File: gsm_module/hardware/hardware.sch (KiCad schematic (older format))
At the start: 33 parts, among them J1 Screw_Terminal_01x04, J2 Programming interface, J3 SWD Debugging Interface, U1 XL1509-5.0, U2 STM32F030F4Px, U3 SIM800C, U4 AMS1117-3.3

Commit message: all but the CANSTACK
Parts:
- removed C10: 100nF, symbol Device:C
- removed C11: 10pF, symbol Device:C
- removed C12: 33pF, symbol Device:C
- removed C9: 330uF, symbol Device:C
- removed R11: 82k, symbol Device:R
- removed U3: SIM800C, RF_GSM:SIMCom_SIM800C, symbol RF_GSM:SIM800C
- added C1, C2: 3.3n, symbol Device:C
- added C4: 100uF, symbol pspice:CAP
- added D2: 1N5820, Diode_THT:D_DO-201AD_P15.24mm_Horizontal, symbol Diode:1N5820
- added D3, D4, D5: LED, symbol Device:LED
- added J2, J3: Conn_01x06_Female, symbol Connector:Conn_01x06_Female
- added JP1, JP2: Jumper, symbol Device:Jumper
- added L2: 68uH, symbol pspice:INDUCTOR
- added R1, R2: 1k, symbol Device:R
- added R13: 100k, symbol Device:R
- added R14: 22k, symbol Device:R
- added R3: 320, symbol Device:R
- added R4: 2.3k, symbol Device:R
- added R5: 330, symbol Device:R
- added U2: XL1509-ADJ, symbol xl1509:XL1509
- added polcap3: 470uF, symbol Device:CP1_Small
- added polcap4: 390uF/6.3v, symbol Device:CP1_Small
- R10: value 100k -> 270k
- R6, R7: value 1k -> 330
- R9: value 330k -> 1k
- U1: value XL1509-5.0 -> XL1509-ADJ
- gave numbers to parts that had none: 2
- renumbered C1 to C3, C4 to C5, C5 to C6, C6 to C7, C7 to C8, C8 to C9, J2 to J4, J3 to J5, JP1 to JP3, JP2 to JP4, R4 to R11, R5 to R12, U4 to U2, U2 to U3
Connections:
- net labels added: 200OK, 4v, NETWORK_ERROR, RESET_PIN, SIM_CARD_ERROR
- wire segments 86 -> 119
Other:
- note removed: "5v to 4V voltage dvider use E12."
- note removed: "ESR=0.7ohm\nsee Hw design p.17 fig.8"
- moved on the sheet: C3, C5, C6, C7, C8, C9, D1, J4, J5, L1, R11, R12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

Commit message: SIM800 Breakout+CANSTACK Rev1 schematic
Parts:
- added C? (x2): 27pF, symbol Device:C
- added JP? (x3): Jumper, symbol Device:Jumper
- added JP?: SPI Jumpers, symbol Device:Jumper
- added R? (x2): 10k, symbol Device:R
- added Y?: 8mhz, symbol Device:Crystal_Small
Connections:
- net labels added: SPI_CSK, SPI_MISO, SPI_MOSI, SPI_NSS
- wire segments 119 -> 136
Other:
- moved on the sheet: C5, C6, C7, C8, C9, J2, J3, J4, J5, R10, R11, R12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

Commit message: Rev 1 schematic all footprints done
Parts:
- removed JP1, JP2, JP? (x3): Jumper, symbol Device:Jumper
- removed JP3, JP4: Programming Jumpers, symbol Device:Jumper
- removed JP?: SPI Jumpers, symbol Device:Jumper
- removed U2: XL1509-ADJ, symbol xl1509:XL1509
- added C11, C5: 5nF, Capacitor_THT:C_Disc_D4.3mm_W1.9mm_P5.00mm, symbol Device:C
- added J10, J11, J12, J13, J6, J7, J8, J9: Conn_01x02_Male, Connector_PinHeader_1.00mm:PinHeader_1x02_P1.00mm_Vertical, symbol Connector:Conn_01x02_Male
- added U10: XL1509-ADJ, Package_SO:SOIC-8-1EP_3.9x4.9mm_P1.27mm_EP2.29x3mm, symbol xl1509:XL1509
- C1, C2: footprint (none) -> Capacitor_THT:C_Disc_D4.3mm_W1.9mm_P5.00mm
- C10: renamed from C9; footprint (none) -> Capacitor_THT:C_Disc_D4.3mm_W1.9mm_P5.00mm
- C12, C13: renamed from C?; footprint (none) -> Capacitor_THT:C_Disc_D4.3mm_W1.9mm_P5.00mm
- C3, C4, polcap1, polcap3, polcap4: footprint (none) -> Capacitor_THT:CP_Radial_D8.0mm_P3.50mm
- C6: renamed from C5; footprint (none) -> Capacitor_THT:C_Disc_D4.3mm_W1.9mm_P5.00mm
- C7: renamed from C6; footprint (none) -> Capacitor_THT:C_Disc_D4.3mm_W1.9mm_P5.00mm
- C8: renamed from C7; footprint (none) -> Capacitor_THT:C_Disc_D4.3mm_W1.9mm_P5.00mm
- C9: renamed from C8; footprint (none) -> Capacitor_THT:C_Disc_D4.3mm_W1.9mm_P5.00mm
- D1, D2: value 1N5820 -> MBR360
- D3, D4, D5: footprint (none) -> LED_THT:LED_D5.0mm
- J1: footprint (none) -> Connector_PinHeader_1.27mm:PinHeader_1x04_P1.27mm_Vertical
- J2: value Conn_01x06_Female -> SIM800C Module; footprint (none) -> Connector_PinHeader_1.27mm:PinHeader_1x06_P1.27mm_Vertical
- J3: value Conn_01x06_Female -> SIM800C Module Side A; footprint (none) -> Connector_PinHeader_1.27mm:PinHeader_1x06_P1.27mm_Vertical
- J4: footprint (none) -> Connector_PinHeader_1.00mm:PinHeader_1x05_P1.00mm_Vertical
- J5: footprint (none) -> Connector_PinHeader_1.00mm:PinHeader_1x02_P1.00mm_Vertical
- L1, L2: footprint (none) -> Resistor_THT:R_Axial_DIN0207_L6.3mm_D2.5mm_P10.16mm_Horizontal
- R1, R10, R11, R2, R3, R4, R5, R6, R7, R8, R9: footprint (none) -> Resistor_THT:R_Axial_DIN0309_L9.0mm_D3.2mm_P12.70mm_Horizontal
- R12: renamed from R13; footprint (none) -> Resistor_THT:R_Axial_DIN0309_L9.0mm_D3.2mm_P12.70mm_Horizontal
- R13: renamed from R14; footprint (none) -> Resistor_THT:R_Axial_DIN0309_L9.0mm_D3.2mm_P12.70mm_Horizontal
- R14: renamed from R12; footprint (none) -> Resistor_THT:R_Axial_DIN0309_L9.0mm_D3.2mm_P12.70mm_Horizontal
- R15, R16: renamed from R?; footprint (none) -> Resistor_THT:R_Axial_DIN0309_L9.0mm_D3.2mm_P12.70mm_Horizontal
- U1: footprint (none) -> Package_SO:SOIC-8-1EP_3.9x4.9mm_P1.27mm_EP2.29x3mm
- Y1: renamed from Y?; footprint (none) -> Crystal:Crystal_HC18-U_Vertical
- renumbered U4 to U3, U3 to U4
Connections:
- wire segments 136 -> 151

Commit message: rev 1.5 final
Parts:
- polcap2: footprint (none) -> Capacitor_THT:CP_Radial_D8.0mm_P3.50mm
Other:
- moved on the sheet: C1, C3, D1, L1, R1, R3, U1A, polcap1, polcap2

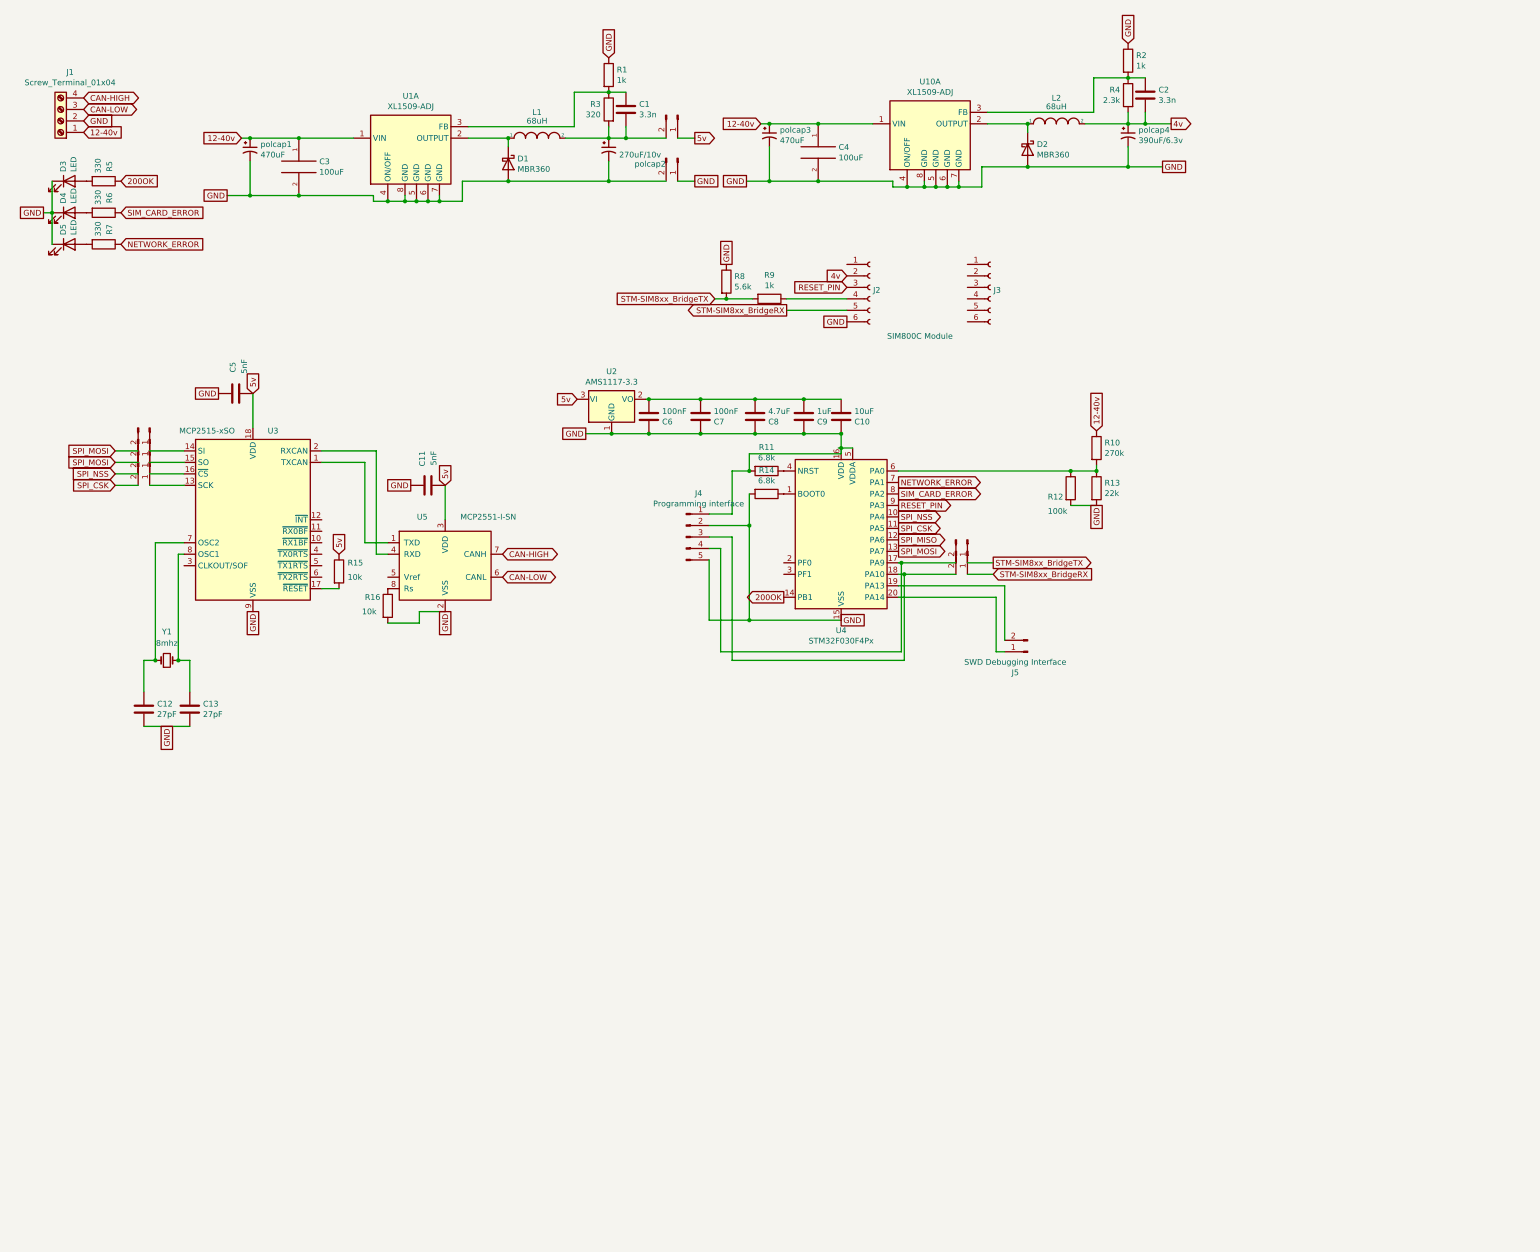
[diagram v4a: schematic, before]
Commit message: rev 1.6 (changed SMT antenna)
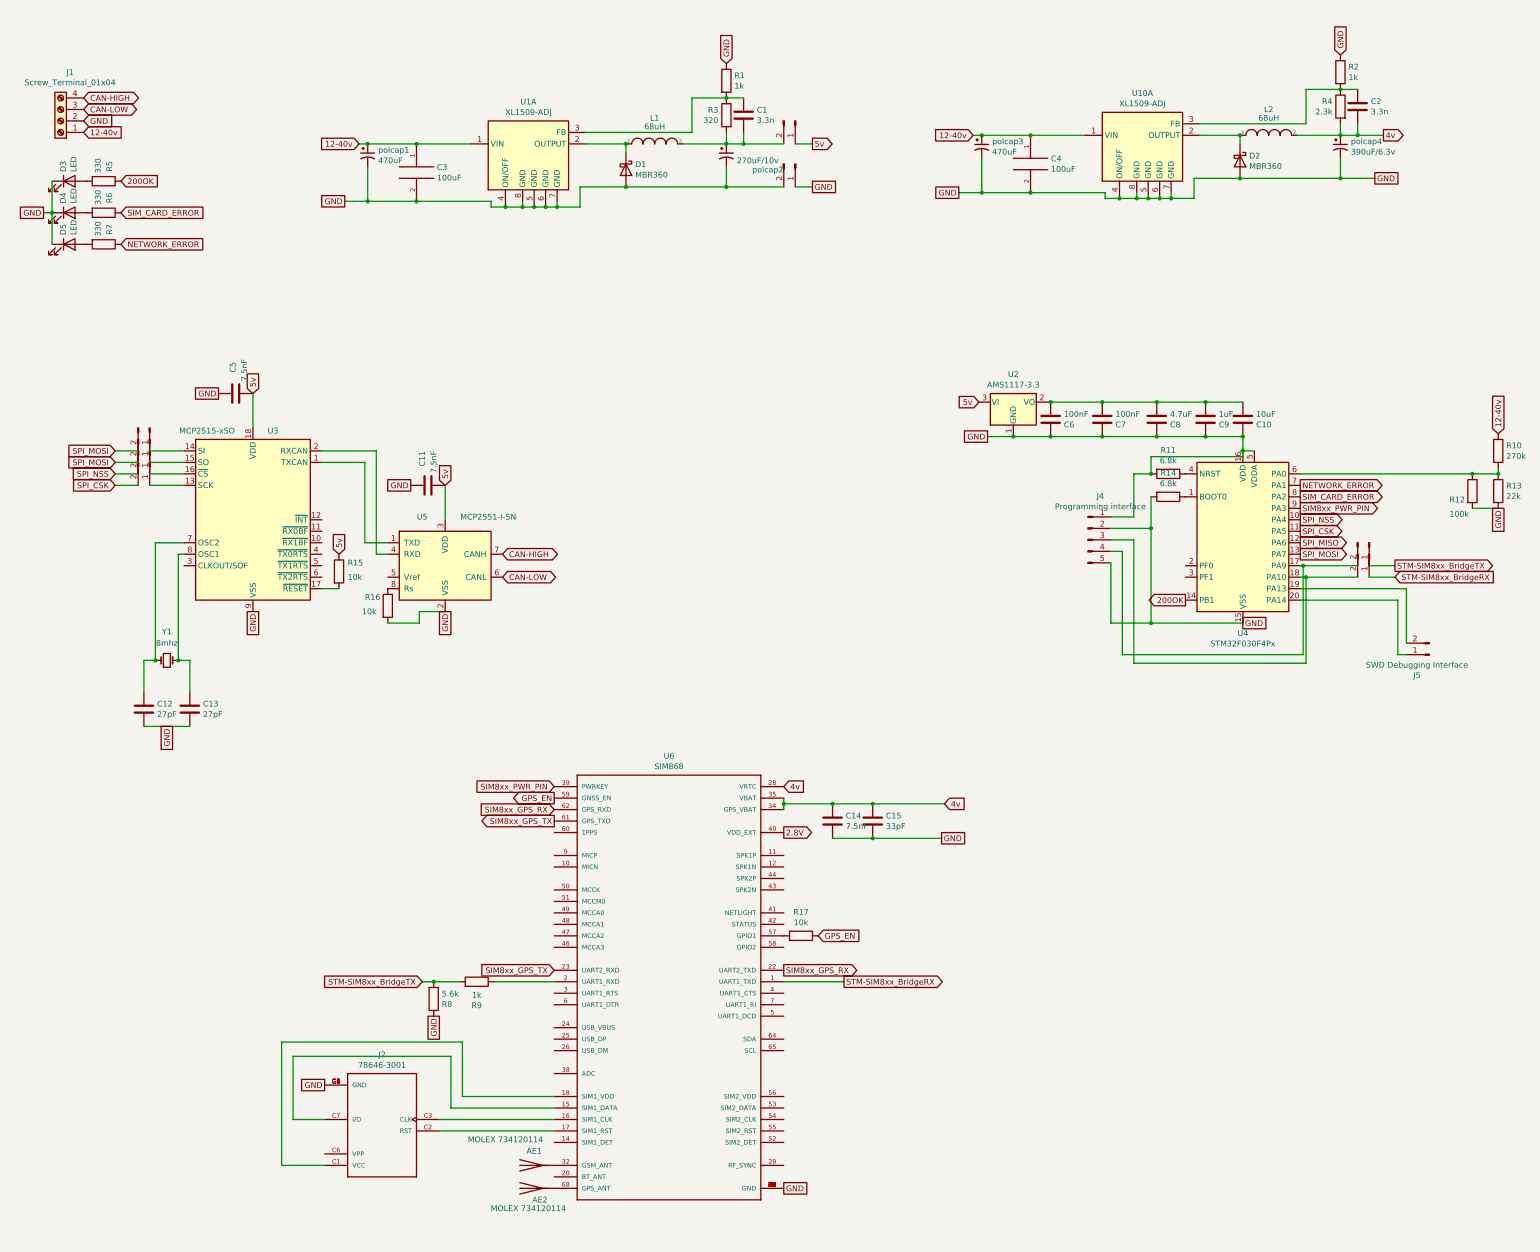
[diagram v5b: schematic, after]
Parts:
- removed J2: SIM800C Module, Connector_PinHeader_1.27mm:PinHeader_1x06_P1.27mm_Vertical, symbol Connector:Conn_01x06_Female
- removed J3: SIM800C Module Side A, Connector_PinHeader_1.27mm:PinHeader_1x06_P1.27mm_Vertical, symbol Connector:Conn_01x06_Female
- added AE1, AE2: MOLEX 734120114, its_app:KH-IPEX4-2020, symbol Device:Antenna
- added C14: 7.5nF, Capacitor_THT:C_Disc_D4.3mm_W1.9mm_P5.00mm, symbol Device:C
- added C15: 33pF, Capacitor_THT:C_Disc_D4.3mm_W1.9mm_P5.00mm, symbol Device:C
- added J2: 78646-3001, its_app:MOLEX_78646-3001, symbol 78646-3001:78646-3001
- added R17: 10k, Resistor_THT:R_Axial_DIN0309_L9.0mm_D3.2mm_P12.70mm_Horizontal, symbol Device:R
- added U6: SIM868, its_app:XCVR_SIM868, symbol SIM868:SIM868
- C11, C5: value 5nF -> 7.5nF
- J1: footprint Connector_PinHeader_1.27mm:PinHeader_1x04_P1.27mm_Vertical -> its_app:5mm Pitch Screw Terminal 1x04
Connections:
- net 4v: now also C14.1, C15.1, U6.28 (VRTC), U6.34 (GPS_VBAT), U6.35 (VBAT)
- net GND: now also C14.2, C15.2, J2.C5 (GND), J2.G1 (GND), J2.G2 (GND), J2.G3 (GND), J2.G4 (GND), J2.G5 (GND), J2.G6 (GND), U6.13 (GND), U6.19 (GND), U6.21 (GND), U6.27 (GND), U6.30 (GND), U6.31 (GND), U6.33 (GND), U6.36 (GND), U6.37 (GND), U6.45 (GND), U6.63 (GND), U6.66 (GND), U6.67 (GND), U6.69 (GND), U6.70 (GND), U6.71 (GND), U6.72 (GND), U6.73 (GND), U6.74 (GND), U6.75 (GND), U6.76 (GND), U6.77 (GND), U6.8 (GND)
- net STM-SIM8xx_BridgeRX: now also U6.1 (UART1_TXD)
- net at R9.1: now also U6.2 (UART1_RXD)
- net RESET_PIN renamed SIM8xx_PWR_PIN
- net SIM8xx_PWR_PIN: now also U6.39 (PWRKEY)
- new net: J2.C7 (I/O), U6.15 (SIM1_DATA)
- new net: J2.C3 (CLK), U6.16 (SIM1_CLK)
- new net: J2.C2 (RST), U6.17 (SIM1_RST)
- new net: J2.C1 (VCC), U6.18 (SIM1_VDD)
- new net: AE1.1 (A), U6.32 (GSM_ANT)
- new net: R17.2, U6.57 (GPIO1)
- new net: AE2.1 (A), U6.68 (GPS_ANT)
- new net 2.8V: U6.40 (VDD_EXT)
- new net GPS_EN: R17.1, U6.59 (GNSS_EN)
- new net SIM8xx_GPS_RX: U6.22 (UART2_TXD), U6.62 (GPS_RXD)
- new net SIM8xx_GPS_TX: U6.23 (UART2_RXD), U6.61 (GPS_TXD)
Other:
- moved on the sheet: C1, C10, C2, C3, C4, C6, C7, C8, C9, D1, D2, J4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

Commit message: rev .5 PCB motherfucker (we-ho)
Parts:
- removed AE1, AE2: MOLEX 734120114, its_app:KH-IPEX4-2020, symbol Device:Antenna
- added U7, U8: MOLEX-734120114, its_app:KH-IPEX4-2020, symbol SIM868:MOLEX-734120114
- J10, J11, J12, J13, J5, J6, J7, J8, J9: footprint Connector_PinHeader_1.00mm:PinHeader_1x02_P1.00mm_Vertical -> Connector_PinHeader_2.54mm:PinHeader_1x02_P2.54mm_Vertical
- J4: footprint Connector_PinHeader_1.00mm:PinHeader_1x05_P1.00mm_Vertical -> Connector_PinHeader_2.54mm:PinHeader_1x05_P2.54mm_Vertical
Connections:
- net GND: now also U7.1 (GND), U8.1 (GND); no longer J4.1 (Pin_1), J4.2 (Pin_2), R11.2, U4.16 (VDD), U4.5 (VDDA)
- net SPI_MISO: now also J9.2 (Pin_2)
- net SPI_MOSI: no longer J9.2 (Pin_2)
- net at R14.1, U4.1 (BOOT0): now also J4.2 (Pin_2)
- net at C10.2, C6.2, C7.2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: now also J4.1 (Pin_1), R11.2, U4.16 (VDD), U4.5 (VDDA)
- net at U6.32 (GSM_ANT): now also U7.2 (Signal)
- net at U6.68 (GPS_ANT): now also U8.2 (Signal)
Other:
- moved on the sheet: C10, C6, C7, C8, C9, U2

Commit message: PCB rev 0.8
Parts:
- removed J7: Conn_01x02_Male, Connector_PinHeader_2.54mm:PinHeader_1x02_P2.54mm_Vertical, symbol Connector:Conn_01x02_Male
- removed U7, U8: MOLEX-734120114, its_app:KH-IPEX4-2020, symbol SIM868:MOLEX-734120114
- removed polcap1, polcap3: 470uF, Capacitor_THT:CP_Radial_D8.0mm_P3.50mm, symbol Device:CP1_Small
- added A1, A2: BWSMA-KE-Z001, its_app:BWSMA-KE-Z001, symbol esortic_hardware_lib:BWSMA-KE-Z001
- C11, C5: value 7.5nF -> 3.3nF
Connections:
- net GND: now also A1.2 (GND), A2.2 (GND)
- net at U6.32 (GSM_ANT): now also A1.1 (Signal)
- net at U6.68 (GPS_ANT): now also A2.1 (Signal)
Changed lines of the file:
@@
 CAN-HIGH
-$Comp
-L Device:CP1_Small polcap1
-U 1 1 5F26D3DB
-P 3525 1775
-F 0 "polcap1" H 3616 1821 50  0000 L CNN
-F 1 "470uF" H 3616 1730 50  0000 L CNN
-F 2 "Capacitor_THT:CP_Radial_D8.0mm_P3.50mm" H 3525 1775 50  0001 C CNN
-F 3 "~" H 3525 1775 50  0001 C CNN
-	1    3525 1775
-	1    0    0    -1
-$EndComp
 $Comp
 L pspice:CAP C3
@@
 12-40v
 Wire Wire Line
-	3450 1675 3525 1675
-Connection ~ 3525 1675
-Wire Wire Line
-	3525 1675 3950 1675
-Wire Wire Line
 	3950 1675 4425 1675
 Connection ~ 3950 1675
-Wire Wire Line
-	3525 2175 3525 1875
-Wire Wire Line
-	3950 2175 3525 2175
 $Comp
 L Diode:1N5820 D1
@@
 GND
 Wire Wire Line
-	3525 2175 3325 2175
-Connection ~ 3525 2175
-Wire Wire Line
 	3950 2175 4600 2175
 Wire Wire Line
@@
 Connection ~ 6650 1675
 Wire Wire Line
-	6650 1875 6650 2050
-Wire Wire Line
 	6275 1675 6650 1675
 Connection ~ 5775 1675
@@
 $EndComp
 $Comp
-L Device:CP1_Small polcap3
-U 1 1 5F2E20E3
-P 8875 1700
-F 0 "polcap3" H 8966 1746 50  0000 L CNN
-F 1 "470uF" H 8966 1655 50  0000 L CNN
-F 2 "Capacitor_THT:CP_Radial_D8.0mm_P3.50mm" H 8875 1700 50  0001 C CNN
-F 3 "~" H 8875 1700 50  0001 C CNN
-	1    8875 1700
-	1    0    0    -1
-$EndComp
-$Comp
 L pspice:CAP C4
 U 1 1 5F2E20E9
@@
 12-40v
 Wire Wire Line
-	8800 1600 8875 1600
-Connection ~ 8875 1600
-Wire Wire Line
-	8875 1600 9300 1600
-Wire Wire Line
 	9300 1600 9775 1600
 Connection ~ 9300 1600
-Wire Wire Line
-	8875 2100 8875 1800
-Wire Wire Line
-	9300 2100 8875 2100
 $Comp
 L Diode:1N5820 D2
@@
 Text GLabel 8675 2100 0    50   UnSpc ~ 0
 GND
-Wire Wire Line
-	8875 2100 8675 2100
-Connection ~ 8875 2100
 Wire Wire Line
 	9300 2100 9950 2100
@@
 Wire Wire Line
 	6800 1675 6650 1675
-Connection ~ 6650 2050
 Text GLabel 2525 5750 3    50   UnSpc ~ 0
 GND
@@
 P 4050 4650
 F 0 "C11" H 3750 4600 50  0000 L CNN
-F 1 "7.5nF" H 3750 4700 50  0000 L CNN
+F 1 "3.3nF" H 3750 4700 50  0000 L CNN
 F 2 "Capacitor_THT:C_Disc_D4.3mm_W1.9mm_P5.00mm" H 4088 4500 50  0001 C CNN
 F 3 "~" H 4050 4650 50  0001 C CNN
@@
 P 2375 3850
 F 0 "C5" H 2100 3825 50  0000 L CNN
-F 1 "7.5nF" H 2075 3925 50  0000 L CNN
+F 1 "3.3nF" H 2075 3925 50  0000 L CNN
 F 2 "Capacitor_THT:C_Disc_D4.3mm_W1.9mm_P5.00mm" H 2413 3700 50  0001 C CNN
 F 3 "~" H 2375 3850 50  0001 C CNN
@@
 	7150 1675 6800 1675
 Connection ~ 6800 1675
-$Comp
-L Connector:Conn_01x02_Male J7
-U 1 1 5F3010C0
-P 7250 1850
-F 0 "J7" V 7312 1894 50  0001 L CNN
-F 1 "Conn_01x02_Male" V 7403 1894 50  0001 L CNN
-F 2 "Connector_PinHeader_2.54mm:PinHeader_1x02_P2.54mm_Vertical" H 7250 1850 50  0001 C CNN
-F 3 "~" H 7250 1850 50  0001 C CNN
-	1    7250 1850
-	0    1    1    0
-$EndComp
-Wire Wire Line
-	7250 2050 7400 2050
-Wire Wire Line
-	6650 2050 7150 2050
 $Comp
 L Connector:Conn_01x02_Male J8
@@
 Wire Wire Line
 	7925 7725 8525 7725
-$Comp
-L SIM868:MOLEX-734120114 U7
-U 1 1 5F31FDE4
-P 4900 10825
-F 0 "U7" H 4900 10452 50  0000 C CNN
-F 1 "MOLEX-734120114" H 4900 10849 50  0001 C CNN
-F 2 "its_app:KH-IPEX4-2020" H 4900 10825 50  0001 C CNN
-F 3 "" H 4900 10825 50  0001 C CNN
-	1    4900 10825
-	-1   0    0    1
-$EndComp
-$Comp
-L SIM868:MOLEX-734120114 U8
-U 1 1 5F32103F
-P 4900 11125
-F 0 "U8" H 4900 10660 50  0000 C CNN
-F 1 "MOLEX-734120114" H 4900 10751 50  0000 C CNN
-F 2 "its_app:KH-IPEX4-2020" H 4900 11125 50  0001 C CNN
-F 3 "" H 4900 11125 50  0001 C CNN
-	1    4900 11125
-	-1   0    0    1
-$EndComp
-Wire Wire Line
-	5150 10875 5150 10775
-Text GLabel 4650 10825 0    50   UnSpc ~ 0
-GND
-Wire Wire Line
-	4650 10675 4650 10975
 Text GLabel 1325 4450 0    50   Input ~ 0
 SPI_MISO
@@
 	10650 5025 10650 4750
 Connection ~ 10650 4750
+$Comp
+L esortic_hardware_lib:BWSMA-KE-Z001 A1
+U 1 1 5F3D96CB
+P 4850 10825
+F 0 "A1" H 4875 11300 50  0000 C CNN
+F 1 "BWSMA-KE-Z001" H 4875 11209 50  0000 C CNN
+F 2 "its_app:BWSMA-KE-Z001" H 4800 10775 50  0001 C CNN
+F 3 "" H 4800 10775 50  0001 C CNN
+	1    4850 10825
+	1    0    0    -1
+$EndComp
+$Comp
+L esortic_hardware_lib:BWSMA-KE-Z001 A2
+U 1 1 5F3D9FB1
+P 4850 11300
+F 0 "A2" H 4875 11775 50  0000 C CNN
+F 1 "BWSMA-KE-Z001" H 4875 11684 50  0000 C CNN
+F 2 "its_app:BWSMA-KE-Z001" H 4800 11250 50  0001 C CNN
+F 3 "" H 4800 11250 50  0001 C CNN
+	1    4850 11300
+	1    0    0    -1
+$EndComp
+Wire Wire Line
+	5150 11050 5150 10775
+Wire Wire Line
+	4600 10725 4600 11200
+Text GLabel 4600 11000 0    50   UnSpc ~ 0
+GND
+Wire Wire Line
+	8800 1600 9300 1600
+Wire Wire Line
+	8675 2100 9300 2100
+Wire Wire Line
+	3450 1675 3950 1675
+Wire Wire Line
+	3325 2175 3950 2175
+Wire Wire Line
+	6650 1875 6650 2050
+Wire Wire Line
+	6650 2050 7400 2050
+Connection ~ 6650 2050
 $EndSCHEMATC
